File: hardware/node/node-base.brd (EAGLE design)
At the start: 100 x 80 mm, 55 parts, among them IC1 HYPERTRIANGLE_TCS3472FN, Q1 32.768kHz, Q2 24MHz, Q3 BS250, U1 INA322_DGK_8, U2 LMV551_DBV_5, X1 BU-SMA-V

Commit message: Finished off routeing by fixing some stuff
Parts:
- moved C7 2.84 mm to (15.2, 21.0), turned to 90 degrees
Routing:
- net GND: track 397.4 -> 359.1 mm
- net +3V3: track 350.2 -> 354.9 mm, vias 5 -> 3
- net RADIO_INT: track 53.2 -> 51.3 mm, vias 3 -> 1
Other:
- board size 100 x 80 mm -> 83.2 x 53.3 mm
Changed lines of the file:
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@@
 <layer number="25" name="tNames" color="7" fill="1" visible="yes" active="yes"/>
 <layer number="26" name="bNames" color="7" fill="1" visible="yes" active="yes"/>
-<layer number="27" name="tValues" color="7" fill="1" visible="no" active="yes"/>
-<layer number="28" name="bValues" color="7" fill="1" visible="no" active="yes"/>
+<layer number="27" name="tValues" color="7" fill="1" visible="yes" active="yes"/>
+<layer number="28" name="bValues" color="7" fill="1" visible="yes" active="yes"/>
 <layer number="29" name="tStop" color="7" fill="3" visible="no" active="yes"/>
 <layer number="30" name="bStop" color="7" fill="6" visible="no" active="yes"/>
@@
 <board>
 <plain>
-<wire x1="0" y1="0" x2="100" y2="0" width="0" layer="20"/>
-<wire x1="100" y1="0" x2="100" y2="80" width="0" layer="20"/>
-<wire x1="100" y1="80" x2="0" y2="80" width="0" layer="20"/>
-<wire x1="0" y1="80" x2="0" y2="0" width="0" layer="20"/>
+<wire x1="0" y1="0" x2="82.855" y2="0" width="0" layer="20"/>
+<wire x1="82.855" y1="0" x2="82.5375" y2="53.33" width="0" layer="20"/>
+<wire x1="82.5375" y1="53.33" x2="-0.3175" y2="53.33" width="0" layer="20"/>
+<wire x1="-0.3175" y1="53.33" x2="0" y2="0" width="0" layer="20"/>
 <wire x1="0" y1="0.635" x2="81.5975" y2="0.635" width="0.4064" layer="249"/>
 <wire x1="81.5975" y1="0.635" x2="81.915" y2="50.165" width="0.4064" layer="249"/>
@@
 <element name="R11" library="resistor" package="0204/7" value="10M" x="52.07" y="36.83"/>
 <element name="C6" library="SparkFun-Capacitors" package="CAP-PTH-SMALL" value="100n" x="40.64" y="27.94" rot="MR180"/>
-<element name="C7" library="SparkFun-Capacitors" package="CAP-PTH-5MM" value="100n" x="17.78" y="19.685" rot="MR180"/>
+<element name="C7" library="SparkFun-Capacitors" package="CAP-PTH-5MM" value="100n" x="15.24" y="20.955" rot="MR90"/>
 <element name="C8" library="SparkFun-Capacitors" package="CAP-PTH-SMALL" value="100n" x="35.8775" y="12.7"/>
 <element name="C9" library="SparkFun-Capacitors" package="CAP-PTH-SMALL" value="100n" x="34.0905" y="30.5515" rot="MR180"/>
@@
 <wire x1="35.8775" y1="14.9225" x2="35.4925" y2="15.3075" width="0.254" layer="16"/>
 <wire x1="35.4925" y1="16.705" x2="35.4925" y2="15.3075" width="0.254" layer="16"/>
-<wire x1="20.955" y1="24.765" x2="19.685" y2="24.765" width="0.4064" layer="16"/>
-<wire x1="19.685" y1="24.765" x2="19.05" y2="24.13" width="0.4064" layer="16"/>
-<wire x1="19.05" y1="24.13" x2="19.05" y2="20.955" width="0.4064" layer="16"/>
-<wire x1="19.05" y1="20.955" x2="20.32" y2="19.685" width="0.4064" layer="16"/>
 <wire x1="38.4175" y1="12.7" x2="38.4175" y2="13.0175" width="0.254" layer="16"/>
 <wire x1="4.445" y1="37.465" x2="4.445" y2="34.925" width="0.4064" layer="16"/>
@@
 <wire x1="17.78" y1="29.845" x2="22.86" y2="29.845" width="0.4064" layer="1"/>
 <wire x1="22.86" y1="24.765" x2="22.86" y2="25.7175" width="0.4064" layer="1"/>
-<wire x1="22.86" y1="25.7175" x2="22.225" y2="26.3525" width="0.4064" layer="1"/>
-<wire x1="22.225" y1="26.3525" x2="19.05" y2="26.3525" width="0.4064" layer="1"/>
-<wire x1="19.05" y1="26.3525" x2="18.0975" y2="25.4" width="0.4064" layer="1"/>
-<wire x1="18.0975" y1="25.4" x2="18.0975" y2="6.0325" width="0.4064" layer="1"/>
-<wire x1="18.0975" y1="6.0325" x2="20.955" y2="3.175" width="0.4064" layer="1"/>
-<wire x1="20.955" y1="3.175" x2="23.255" y2="3.175" width="0.4064" layer="1"/>
 <wire x1="23.255" y1="3.175" x2="23.5575" y2="3.4775" width="0.4064" layer="1"/>
 <wire x1="38.4175" y1="12.7" x2="39.0525" y2="12.7" width="0.4064" layer="1"/>
@@
 <wire x1="36.03625" y1="25.24875" x2="36.03625" y2="29.95725" width="0.254" layer="16"/>
 <wire x1="36.03625" y1="29.95725" x2="36.6305" y2="30.5515" width="0.254" layer="16"/>
-<polygon width="0.254" layer="16" isolate="0.4064">
+<polygon width="0.254" layer="16" isolate="0.6096">
 <vertex x="0.635" y="1.27"/>
 <vertex x="0.9525" y="0.9525"/>
@@
 <vertex x="0.635" y="48.895"/>
 </polygon>
-<polygon width="0.254" layer="1" isolate="0.4064">
+<polygon width="0.254" layer="1" isolate="0.6096">
 <vertex x="0.635" y="48.895"/>
 <vertex x="0.635" y="1.27"/>
@@
 <wire x1="68.58" y1="32.0675" x2="68.58" y2="39.37" width="0.4064" layer="16"/>
 <wire x1="35.480625" y1="25.216875" x2="35.4925" y2="25.205" width="0.254" layer="16"/>
-<wire x1="30.9725" y1="19.685" x2="30.9925" y2="19.705" width="0.254" layer="16"/>
 <wire x1="34.9925" y1="16.705" x2="34.9925" y2="14.5375" width="0.254" layer="16"/>
 <wire x1="45.72" y1="34.925" x2="45.72" y2="37.7825" width="0.4064" layer="16"/>
@@
 <wire x1="14.605" y1="40.64" x2="2.8575" y2="40.64" width="0.4064" layer="1"/>
 <wire x1="2.8575" y1="40.64" x2="1.905" y2="39.6875" width="0.4064" layer="1"/>
-<wire x1="1.905" y1="39.6875" x2="1.905" y2="17.78" width="0.4064" layer="1"/>
-<wire x1="1.905" y1="17.78" x2="1.905" y2="5.63" width="0.4064" layer="1"/>
-<wire x1="1.905" y1="5.63" x2="4.0575" y2="3.4775" width="0.4064" layer="1"/>
-<wire x1="15.28" y1="19.685" x2="15.28" y2="18.1375" width="0.4064" layer="16"/>
-<wire x1="15.28" y1="18.1375" x2="15.24" y2="18.0975" width="0.4064" layer="16"/>
-<via x="15.24" y="18.0975" extent="1-16" drill="0.6096"/>
-<wire x1="15.24" y1="18.0975" x2="14.605" y2="17.4625" width="0.4064" layer="1"/>
-<wire x1="14.605" y1="17.4625" x2="2.2225" y2="17.4625" width="0.4064" layer="1"/>
-<wire x1="2.2225" y1="17.4625" x2="1.905" y2="17.78" width="0.4064" layer="1"/>
-<wire x1="30.9725" y1="19.685" x2="23.1775" y2="19.685" width="0.254" layer="16"/>
-<wire x1="23.1775" y1="19.685" x2="22.86" y2="19.3675" width="0.254" layer="16"/>
-<via x="22.86" y="19.3675" extent="1-16" drill="0.6096"/>
-<wire x1="22.86" y1="19.3675" x2="19.685" y2="16.1925" width="0.254" layer="1"/>
-<via x="19.685" y="16.1925" extent="1-16" drill="0.6096"/>
-<wire x1="19.685" y1="16.1925" x2="16.1925" y2="16.1925" width="0.254" layer="16"/>
-<wire x1="16.1925" y1="16.1925" x2="15.875" y2="16.51" width="0.254" layer="16"/>
-<wire x1="15.875" y1="16.51" x2="15.875" y2="17.4625" width="0.254" layer="16"/>
-<wire x1="15.875" y1="17.4625" x2="15.24" y2="18.0975" width="0.254" layer="16"/>
+<wire x1="1.905" y1="39.6875" x2="1.905" y2="17.145" width="0.4064" layer="1"/>
+<wire x1="1.905" y1="17.145" x2="1.905" y2="5.63" width="0.4064" layer="1"/>
 <wire x1="70.8025" y1="15.875" x2="73.025" y2="15.875" width="0.4064" layer="16"/>
 <wire x1="73.025" y1="15.875" x2="73.025" y2="3.81" width="0.4064" layer="1"/>
 <wire x1="73.025" y1="3.81" x2="71.12" y2="1.905" width="0.4064" layer="1"/>
 <wire x1="71.12" y1="1.905" x2="5.3975" y2="1.905" width="0.4064" layer="1"/>
-<wire x1="5.3975" y1="1.905" x2="4.1275" y2="3.175" width="0.4064" layer="1"/>
-<wire x1="3.81" y1="3.4925" x2="4.1275" y2="3.175" width="0.4064" layer="1"/>
-<wire x1="4.1275" y1="3.175" x2="4.1275" y2="3.4925" width="0.4064" layer="1"/>
 <via x="73.025" y="15.875" extent="1-16" drill="0.6096"/>
 <wire x1="72.3675" y1="12.065" x2="71.755" y2="12.065" width="0.254" layer="16"/>
@@
 <wire x1="34.925" y1="16.7725" x2="34.925" y2="17.78" width="0.254" layer="16"/>
 <wire x1="34.925" y1="17.78" x2="34.6075" y2="18.0975" width="0.254" layer="16"/>
-<wire x1="4.1275" y1="3.4925" x2="4.0575" y2="3.4775" width="0" layer="19" extent="1-1"/>
+<wire x1="53.0225" y1="6.6675" x2="55.5625" y2="6.6675" width="0.4064" layer="16"/>
+<wire x1="55.5625" y1="6.6675" x2="57.4675" y2="8.5725" width="0.4064" layer="16"/>
+<wire x1="57.4675" y1="8.5725" x2="57.4675" y2="14.605" width="0.4064" layer="16"/>
+<wire x1="57.4675" y1="14.605" x2="58.7375" y2="15.875" width="0.4064" layer="16"/>
+<wire x1="58.7375" y1="15.875" x2="70.8025" y2="15.875" width="0.4064" layer="16"/>
+<wire x1="1.905" y1="5.63" x2="4.0575" y2="3.4775" width="0.4064" layer="1"/>
+<wire x1="4.0575" y1="3.4775" x2="4.0575" y2="3.245" width="0.4064" layer="1"/>
+<wire x1="4.0575" y1="3.245" x2="5.3975" y2="1.905" width="0.4064" layer="1"/>
+<wire x1="15.24" y1="18.455" x2="14.3275" y2="18.455" width="0.4064" layer="16"/>
+<wire x1="14.3275" y1="18.455" x2="13.335" y2="17.4625" width="0.4064" layer="16"/>
+<wire x1="13.335" y1="17.4625" x2="11.7475" y2="17.4625" width="0.4064" layer="16"/>
+<via x="11.7475" y="17.4625" extent="1-16" drill="0.6"/>
+<wire x1="11.7475" y1="17.4625" x2="2.2225" y2="17.4625" width="0.4064" layer="1"/>
+<wire x1="2.2225" y1="17.4625" x2="1.905" y2="17.145" width="0.4064" layer="1"/>
 </signal>
 <signal name="DETECT_REF">
@@
 <wire x1="27.6225" y1="22.5425" x2="23.1775" y2="18.0975" width="0.254" layer="1"/>
 <wire x1="23.1775" y1="18.0975" x2="22.5425" y2="18.0975" width="0.254" layer="1"/>
-<wire x1="22.5425" y1="18.0975" x2="20.955" y2="16.51" width="0.254" layer="1"/>
-<wire x1="20.955" y1="16.51" x2="20.955" y2="14.9225" width="0.254" layer="1"/>
-<wire x1="20.955" y1="14.9225" x2="20.32" y2="14.2875" width="0.254" layer="1"/>
-<via x="20.32" y="14.2875" extent="1-16" drill="0.6096"/>
-<wire x1="20.32" y1="14.2875" x2="15.875" y2="14.2875" width="0.254" layer="16"/>
-<via x="15.875" y="14.2875" extent="1-16" drill="0.6096"/>
-<wire x1="15.875" y1="14.2875" x2="5.2475" y2="14.2875" width="0.254" layer="1"/>
-<wire x1="5.2475" y1="14.2875" x2="4.0575" y2="15.4775" width="0.254" layer="1"/>
+<wire x1="22.5425" y1="18.0975" x2="19.9225" y2="15.4775" width="0.254" layer="1"/>
+<wire x1="4.0575" y1="15.4775" x2="19.9225" y2="15.4775" width="0.254" layer="1"/>
 </signal>
 <signal name="EXT_PWRLINE">

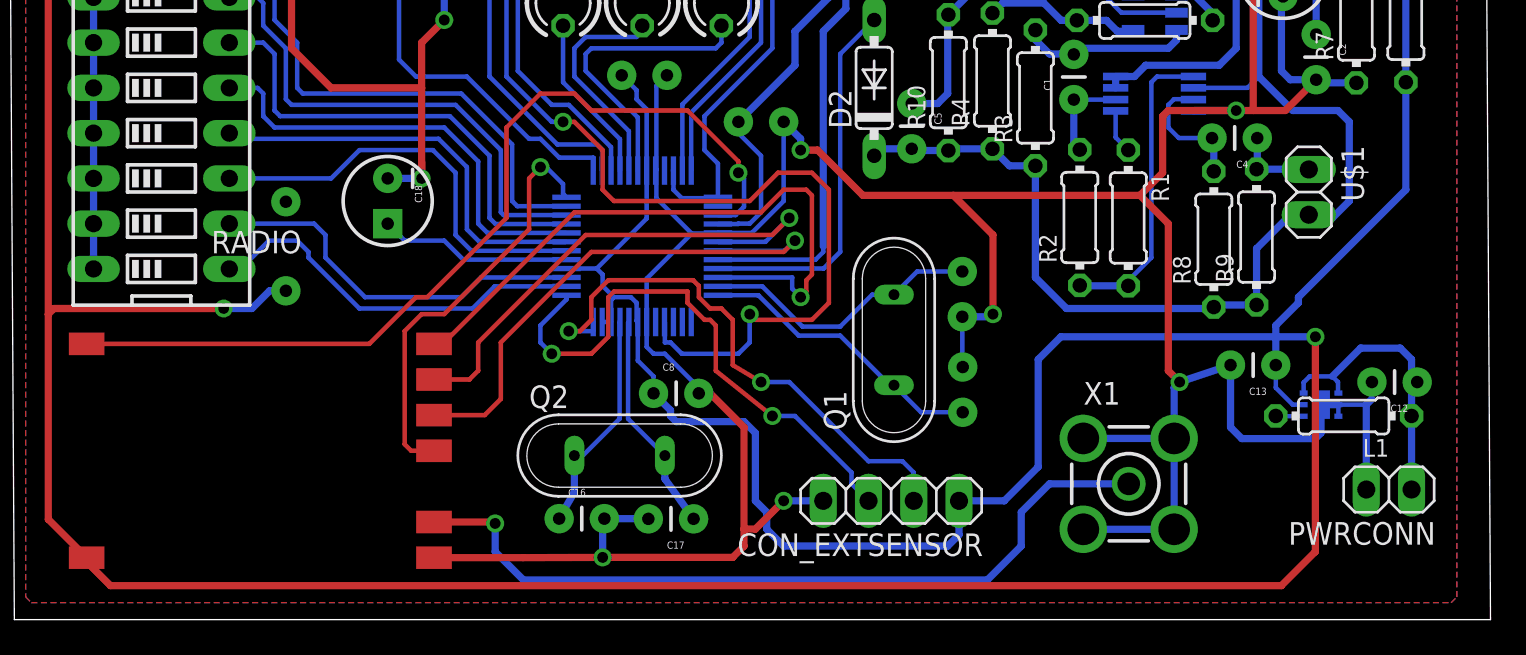
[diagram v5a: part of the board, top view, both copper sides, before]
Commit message: NODEHW: PSU layout now looks like TI's
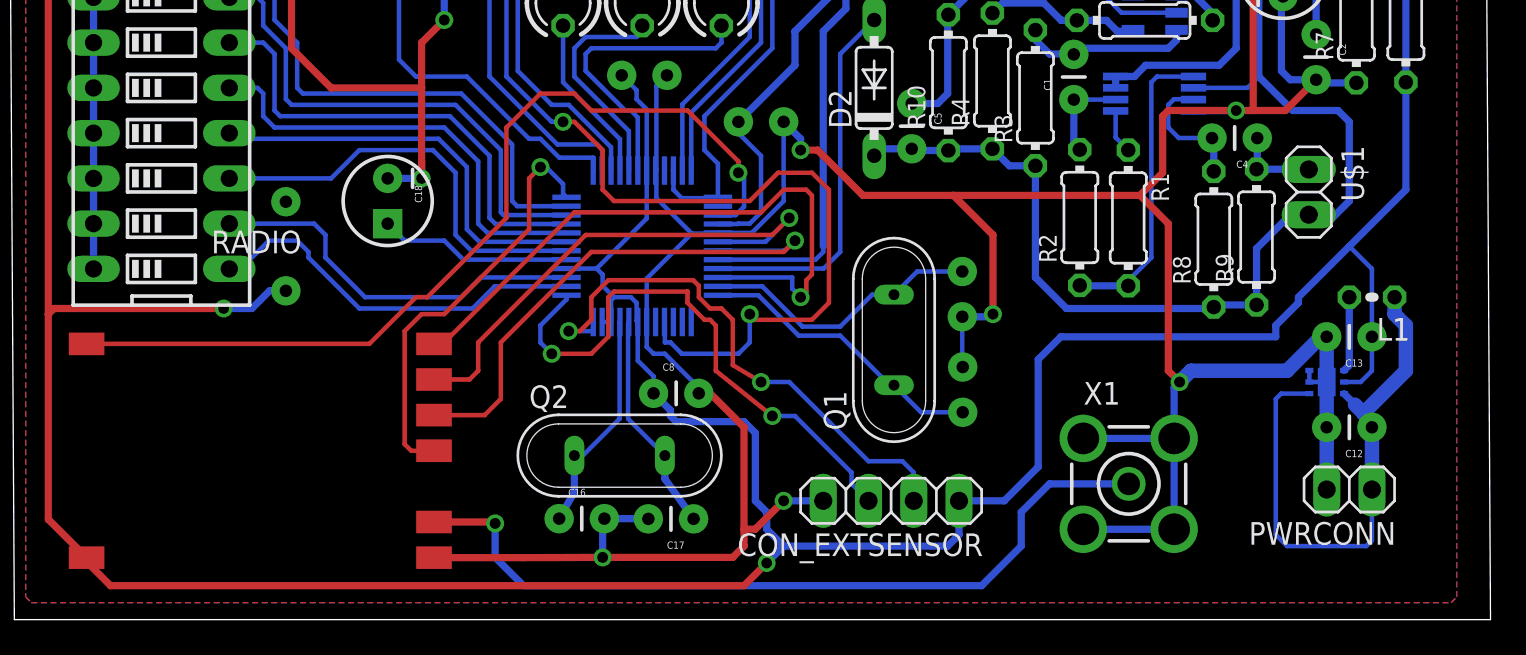
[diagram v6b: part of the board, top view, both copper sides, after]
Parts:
- L1: device resistor:0204/7 -> resistor:0204V
- moved L1 6.85 mm to (76.2, 18.1)
- moved C13 5.63 mm to (76.2, 15.9)
- moved C12 3.59 mm to (76.2, 10.8)
- moved PWRCONN 2.22 mm to (74.9, 7.30)
- moved U$4 1.31 mm to (73.7, 13.3), turned to 0 degrees
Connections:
- net N$4 renamed VREG_SW
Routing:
- net +3V3: track 354.9 -> 315.4 mm
- net V+: track 16.5 -> 33.7 mm
- net VREG_SW: track 1.57 -> 4.23 mm
- net GND: track 359.1 -> 357.0 mm
- added copper zone on layer 16, net +3V3

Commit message: NODEHW: Layout cleanup. Also added base text
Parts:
- moved C18 1.59 mm to (21.0, 21.9)
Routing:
- net GND: track 357.0 -> 359.5 mm, vias 12 -> 16
- net +3V3: track 315.4 -> 317.4 mm
- net DECOUPLE: track 10.9 -> 10.2 mm
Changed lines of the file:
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@@
 <wire x1="-0.3175" y1="53.33" x2="0" y2="0" width="0" layer="20"/>
 <wire x1="0" y1="0.635" x2="81.5975" y2="0.635" width="0.4064" layer="249"/>
-<wire x1="81.5975" y1="0.635" x2="81.915" y2="50.165" width="0.4064" layer="249"/>
-<wire x1="81.915" y1="50.165" x2="0" y2="50.165" width="0.4064" layer="249"/>
-<wire x1="0" y1="50.165" x2="0" y2="0.635" width="0.4064" layer="249"/>
+<wire x1="81.5975" y1="0.635" x2="81.915" y2="49.8475" width="0.4064" layer="249"/>
+<wire x1="81.915" y1="49.8475" x2="0" y2="49.8475" width="0.4064" layer="249"/>
+<wire x1="0" y1="49.8475" x2="0" y2="0.635" width="0.4064" layer="249"/>
 </plain>
 <attributes>
@@
 <param name="mdSmdStop" value="0mil"/>
 <param name="msWidth" value="10mil"/>
-<param name="msDrill" value="24mil"/>
+<param name="msDrill" value="23mil"/>
 <param name="msMicroVia" value="9.99mm"/>
 <param name="msBlindViaRatio" value="0.5"/>
@@
 <element name="C16" library="SparkFun-Capacitors" package="CAP-PTH-SMALL" value="7p5" x="30.578" y="5.667"/>
 <element name="C17" library="SparkFun-Capacitors" package="CAP-PTH-SMALL" value="7p5" x="38.125" y="5.655" rot="R180"/>
-<element name="C18" library="SparkFun-Capacitors" package="CPOL-RADIAL-10UF-25V" value="10u" x="20.955" y="23.495" rot="R270"/>
+<element name="C18" library="SparkFun-Capacitors" package="CPOL-RADIAL-10UF-25V" value="10u" x="20.955" y="21.9075" rot="R270"/>
 <element name="S1(DNF)" library="SparkFun-Electromechanical" package="TACTILE-PTH-EZ" value="SPSTPTH_EZ" x="28.575" y="44.1325"/>
 <element name="RADIO" library="Moteino" package="RFM69W-MINPADS" value="RFM69" x="15.5575" y="10.4775"/>
@@
 <wire x1="43.18" y1="27.94" x2="43.18" y2="23.495" width="0.254" layer="16"/>
 <wire x1="43.18" y1="23.495" x2="41.39" y2="21.705" width="0.254" layer="16"/>
-<wire x1="20.955" y1="24.765" x2="22.86" y2="24.765" width="0.4064" layer="16"/>
 <via x="22.86" y="24.765" extent="1-16" drill="0.6096"/>
 <wire x1="22.86" y1="24.765" x2="22.86" y2="29.845" width="0.4064" layer="1"/>
@@
 <wire x1="35.4925" y1="16.705" x2="35.4925" y2="19.14125" width="0.254" layer="16"/>
 <wire x1="35.4925" y1="19.14125" x2="38.020625" y2="21.669375" width="0.254" layer="16"/>
-<wire x1="4.445" y1="37.465" x2="4.445" y2="39.0525" width="0.4064" layer="16"/>
-<via x="4.445" y="39.0525" extent="1-16" drill="0.6096"/>
-<wire x1="4.445" y1="39.0525" x2="13.6525" y2="39.0525" width="0.4064" layer="1"/>
-<wire x1="13.6525" y1="39.0525" x2="15.5575" y2="37.1475" width="0.4064" layer="1"/>
+<wire x1="4.445" y1="37.465" x2="4.445" y2="40.3225" width="0.4064" layer="16"/>
+<via x="4.445" y="40.3225" extent="1-16" drill="0.6096"/>
+<wire x1="4.445" y1="40.3225" x2="13.97" y2="40.3225" width="0.4064" layer="1"/>
 <wire x1="15.5575" y1="37.1475" x2="15.5575" y2="32.0675" width="0.4064" layer="1"/>
 <wire x1="15.5575" y1="32.0675" x2="17.78" y2="29.845" width="0.4064" layer="1"/>
@@
 <wire x1="22.4914" y1="46.3931" x2="22.309" y2="46.5755" width="0.4064" layer="16"/>
 <wire x1="22.309" y1="46.5755" x2="20.5405" y2="46.5755" width="0.4064" layer="16"/>
-<wire x1="20.5405" y1="46.5755" x2="13.6525" y2="39.6875" width="0.4064" layer="16"/>
-<wire x1="13.6525" y1="39.6875" x2="5.08" y2="39.6875" width="0.4064" layer="16"/>
-<wire x1="5.08" y1="39.6875" x2="4.445" y2="39.0525" width="0.4064" layer="16"/>
+<wire x1="20.5405" y1="46.5755" x2="13.6525" y2="40.9575" width="0.4064" layer="16"/>
+<wire x1="13.6525" y1="40.9575" x2="5.08" y2="40.9575" width="0.4064" layer="16"/>
 <wire x1="59.9976" y1="5.0701" x2="65.0974" y2="5.0701" width="0.4064" layer="16"/>
 <wire x1="65.405" y1="4.7625" x2="65.0974" y2="5.0701" width="0.4064" layer="16"/>
@@
 <polygon width="0.254" layer="16" isolate="0.6096" rank="3">
 <vertex x="0.635" y="1.27"/>
-<vertex x="0.9525" y="0.9525"/>
-<vertex x="80.645" y="0.9525"/>
 <vertex x="80.9625" y="1.27"/>
-<vertex x="80.9625" y="48.5775"/>
-<vertex x="80.645" y="48.895"/>
+<vertex x="80.9625" y="48.895"/>
 <vertex x="0.635" y="48.895"/>
 </polygon>
@@
 <vertex x="0.635" y="48.895"/>
 <vertex x="0.635" y="1.27"/>
-<vertex x="0.9525" y="0.9525"/>
-<vertex x="80.645" y="0.9525"/>
 <vertex x="80.9625" y="1.27"/>
-<vertex x="80.9625" y="48.5775"/>
-<vertex x="80.645" y="48.895"/>
+<vertex x="80.9625" y="48.895"/>
 </polygon>
 <wire x1="65.4098" y1="9.8575" x2="65.0974" y2="10.1699" width="0.254" layer="16"/>
@@
 <wire x1="66.2041" y1="28.575" x2="66.1824" y2="28.5533" width="0.4064" layer="16"/>
 <wire x1="69.5325" y1="28.575" x2="68.58" y2="28.575" width="0.4064" layer="1"/>
+<wire x1="22.86" y1="24.765" x2="22.5425" y2="24.765" width="0.6096" layer="16"/>
+<wire x1="22.5425" y1="24.765" x2="20.955" y2="23.1775" width="0.6096" layer="16"/>
+<wire x1="13.97" y1="40.3225" x2="13.97" y2="38.735" width="0.4064" layer="1"/>
+<wire x1="13.97" y1="38.735" x2="15.5575" y2="37.1475" width="0.4064" layer="1"/>
+<wire x1="4.445" y1="40.3225" x2="5.08" y2="40.9575" width="0.4064" layer="16"/>
+<via x="8.255" y="45.4025" extent="1-16" drill="0.6"/>
+<via x="71.4375" y="44.7675" extent="1-16" drill="0.6"/>
+<via x="78.74" y="2.8575" extent="1-16" drill="0.6"/>
+<via x="26.3525" y="8.5725" extent="1-16" drill="0.6"/>
 </signal>
 <signal name="VCC/2">
@@
 <wire x1="17.78" y1="38.4175" x2="16.8275" y2="39.37" width="0.4064" layer="16"/>
 <via x="16.8275" y="39.37" extent="1-16" drill="0.6096"/>
-<wire x1="16.8275" y1="39.37" x2="15.875" y2="39.37" width="0.4064" layer="1"/>
-<wire x1="15.875" y1="39.37" x2="14.605" y2="40.64" width="0.4064" layer="1"/>
-<wire x1="14.605" y1="40.64" x2="2.8575" y2="40.64" width="0.4064" layer="1"/>
-<wire x1="2.8575" y1="40.64" x2="1.905" y2="39.6875" width="0.4064" layer="1"/>
-<wire x1="1.905" y1="39.6875" x2="1.905" y2="17.145" width="0.4064" layer="1"/>
-<wire x1="1.905" y1="17.145" x2="1.905" y2="5.63" width="0.4064" layer="1"/>
+<wire x1="14.605" y1="41.5925" x2="2.2225" y2="41.5925" width="0.4064" layer="1"/>
+<wire x1="1.905" y1="41.275" x2="1.905" y2="16.8275" width="0.4064" layer="1"/>
+<wire x1="1.905" y1="16.8275" x2="1.905" y2="5.63" width="0.4064" layer="1"/>
 <wire x1="34.925" y1="16.7725" x2="34.925" y2="17.78" width="0.254" layer="16"/>
 <wire x1="34.925" y1="17.78" x2="34.6075" y2="18.0975" width="0.254" layer="16"/>
@@
 <wire x1="58.7375" y1="15.875" x2="70.8025" y2="15.875" width="0.4064" layer="16"/>
 <wire x1="1.905" y1="5.63" x2="4.0575" y2="3.4775" width="0.4064" layer="1"/>
-<wire x1="15.24" y1="18.455" x2="14.3275" y2="18.455" width="0.4064" layer="16"/>
-<wire x1="14.3275" y1="18.455" x2="13.335" y2="17.4625" width="0.4064" layer="16"/>
-<wire x1="13.335" y1="17.4625" x2="11.7475" y2="17.4625" width="0.4064" layer="16"/>
-<via x="11.7475" y="17.4625" extent="1-16" drill="0.6"/>
-<wire x1="11.7475" y1="17.4625" x2="2.2225" y2="17.4625" width="0.4064" layer="1"/>
-<wire x1="2.2225" y1="17.4625" x2="1.905" y2="17.145" width="0.4064" layer="1"/>
+<via x="11.7475" y="16.8275" extent="1-16" drill="0.6"/>
+<wire x1="11.7475" y1="16.8275" x2="1.905" y2="16.8275" width="0.4064" layer="1"/>
 <wire x1="4.0575" y1="3.4775" x2="4.0575" y2="3.245" width="0.4064" layer="1"/>
 <wire x1="4.0575" y1="3.245" x2="5.3975" y2="1.905" width="0.4064" layer="1"/>
@@
 <vertex x="76.835" y="16.1925"/>
 </polygon>
+<wire x1="14.605" y1="41.5925" x2="16.8275" y2="39.37" width="0.4064" layer="1"/>
+<wire x1="2.2225" y1="41.5925" x2="1.905" y2="41.275" width="0.4064" layer="1"/>
+<wire x1="15.24" y1="18.455" x2="15.24" y2="18.0975" width="0.4064" layer="16"/>
+<wire x1="15.24" y1="18.0975" x2="13.97" y2="16.8275" width="0.4064" layer="16"/>
+<wire x1="13.97" y1="16.8275" x2="11.7475" y2="16.8275" width="0.4064" layer="16"/>
 </signal>
 <signal name="DETECT_REF">
@@
 <contactref element="C18" pad="1"/>
 <contactref element="U$2" pad="29"/>
-<wire x1="30.9925" y1="20.205" x2="25.1975" y2="20.205" width="0.254" layer="16"/>
-<wire x1="25.1975" y1="20.205" x2="24.13" y2="21.2725" width="0.254" layer="16"/>
-<wire x1="24.13" y1="21.2725" x2="21.9075" y2="21.2725" width="0.254" layer="16"/>
-<wire x1="21.9075" y1="21.2725" x2="20.955" y2="22.225" width="0.254" layer="16"/>
+<wire x1="30.9925" y1="20.205" x2="21.3875" y2="20.205" width="0.254" layer="16"/>
+<wire x1="21.3875" y1="20.205" x2="20.955" y2="20.6375" width="0.254" layer="16"/>
 </signal>
 <signal name="RADIO_ANT">
